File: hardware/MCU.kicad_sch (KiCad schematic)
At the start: 17 parts

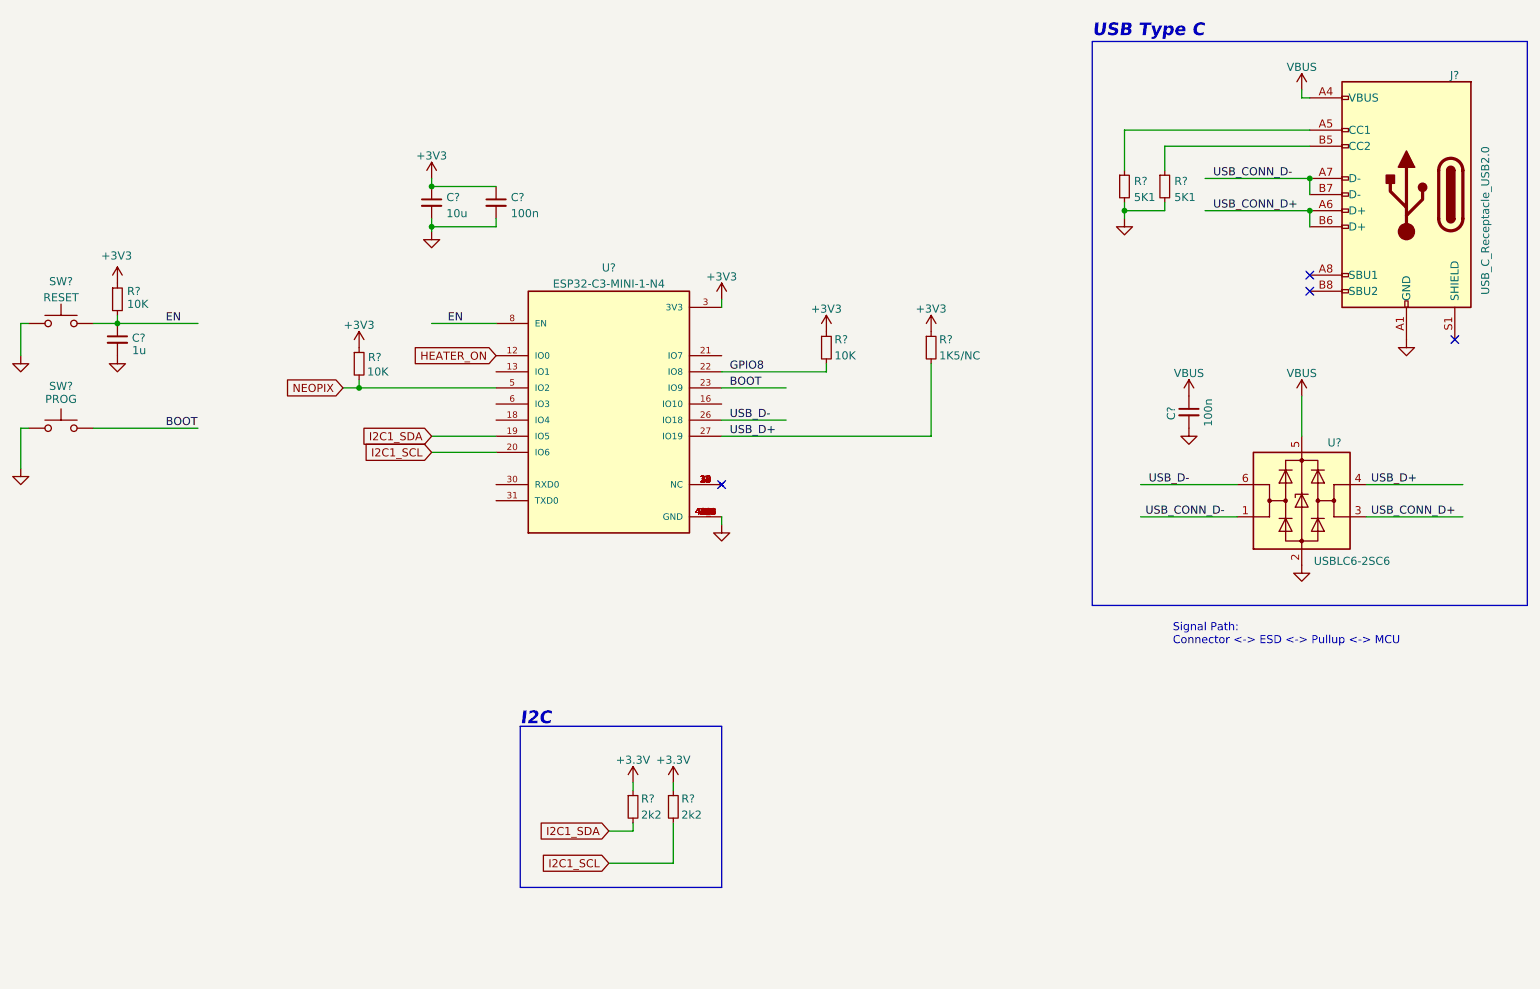
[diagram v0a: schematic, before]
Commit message: schematics finished, footprints assigned. Still need to fix foorptints for MOSFETS
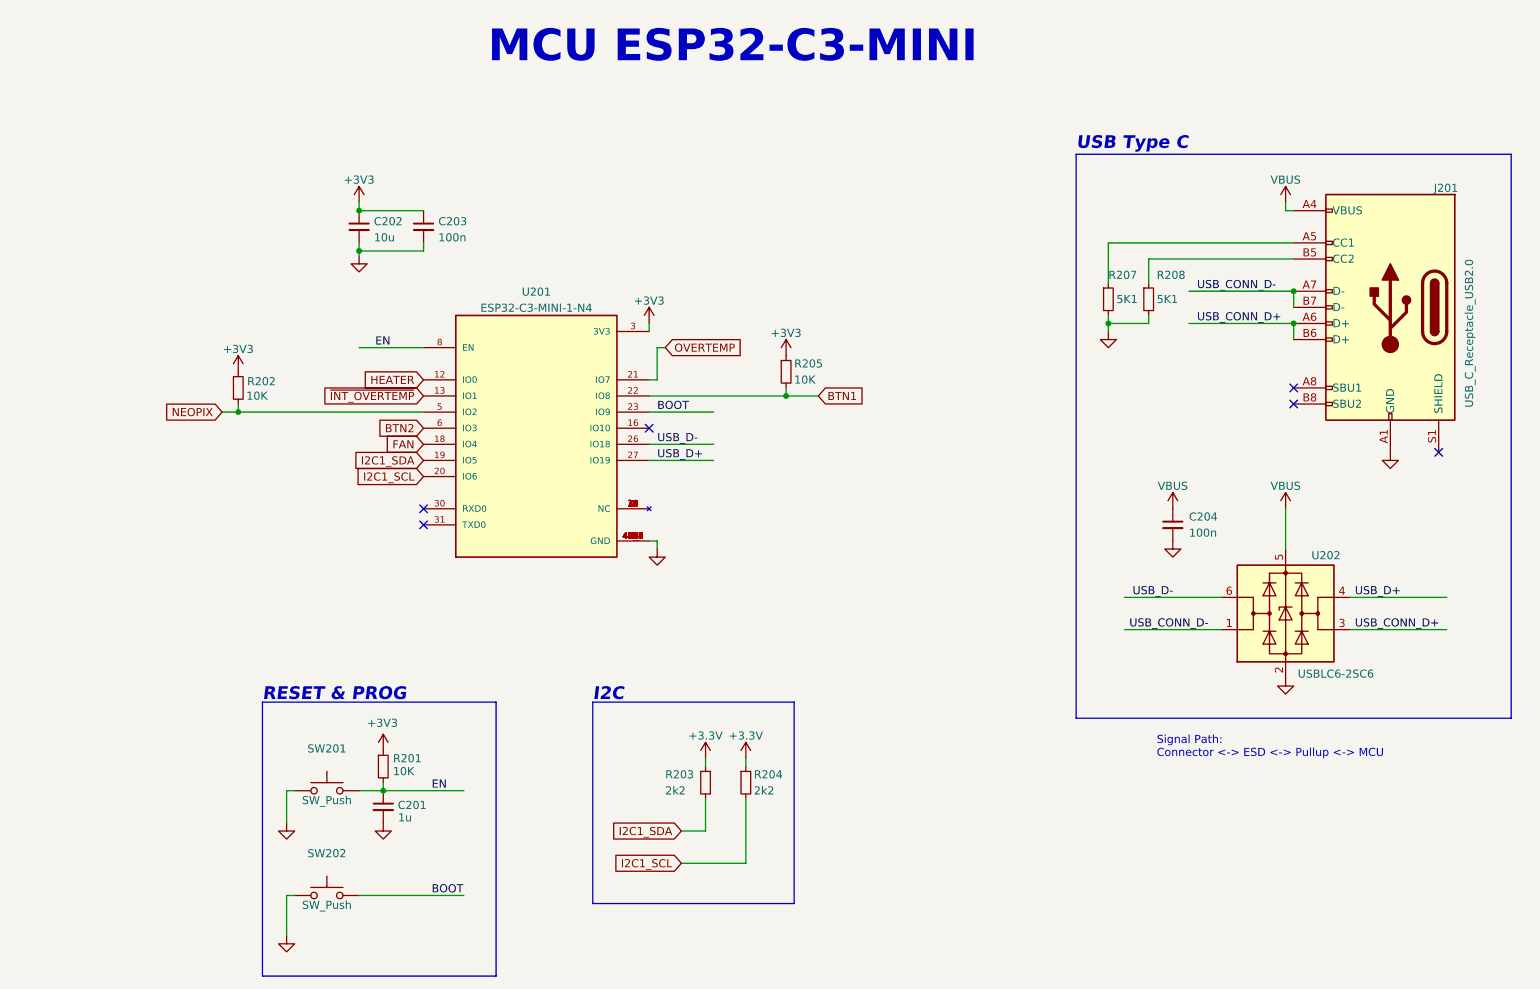
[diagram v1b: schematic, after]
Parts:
- removed R?: 1K5/NC, Resistor_SMD:R_0402_1005Metric, symbol Device:R_Small
- J201: renamed from J?; footprint (none) -> STR-USB:USB_C_Receptacle_C136423
- SW201: renamed from SW?; value RESET -> SW_Push; footprint (none) -> STR-Switch:SW_SMD_SPST_8x3.6; symbol Switch:SW_Push -> STR-Switches:SW_Push
- SW202: renamed from SW?; value PROG -> SW_Push; footprint (none) -> STR-Switch:SW_SMD_SPST_8x3.6; symbol Switch:SW_Push -> STR-Switches:SW_Push
- U201: renamed from U?; footprint esp:ESP32-C3-MINI-1-N4 -> STR-ESP32:ESP32-C3-MINI-1-N4; LCSC (none) -> C2838502; MFPN (none) -> ESP32-C3-MINI-1-N4
- U202: renamed from U?; LCSC (none) -> C2827654; MANUFACTURER (none) -> TECH PUBLIC; MFN (none) -> TECH PUBLIC; MFPN (none) -> USBLC6-2SC6
- gave numbers to parts that had none: 11
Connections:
- net ~{INT_OVERTEMP}: now reaches U201.13 (IO1)
- net FAN: now reaches U201.18 (IO4)
- net OVERTEMP: now reaches U201.21 (IO7)
- net BTN2: now reaches U201.6 (IO3)
- net GPIO8 renamed BTN1
- net HEATER_ON renamed HEATER
- no-connect marks 4 -> 6
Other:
- note added: "MCU ESP32-C3-MINI"
- note added: "RESET & PROG"
- title: (none) -> SLA Chamber Hearter for Resin Printers
- moved on the sheet: C201, C202, C203, C204, J201, R201, R202, R203, R204, R205, R207, R208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

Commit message: routing and foot print changes
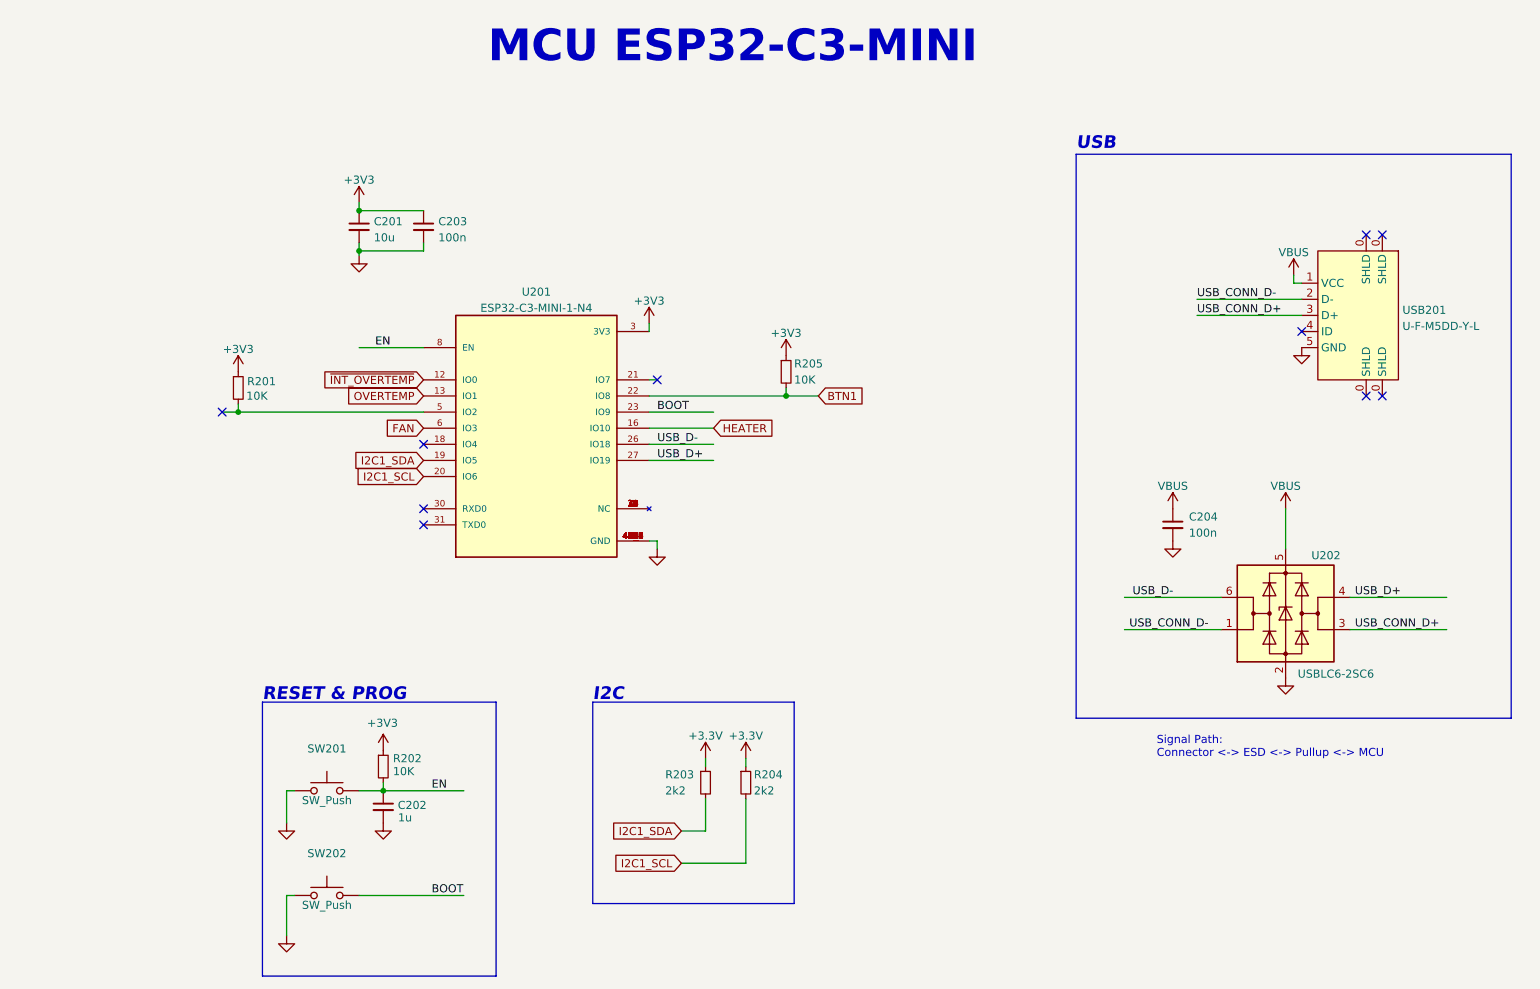
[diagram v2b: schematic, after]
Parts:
- removed J201: USB_C_Receptacle_USB2.0, STR-USB:USB_C_Receptacle_C136423, symbol Connector:USB_C_Receptacle_USB2.0
- removed R207, R208: 5K1, Resistor_SMD:R_0402_1005Metric, symbol Device:R_Small
- added USB201: U-F-M5DD-Y-L, STR-USB:MICRO-USB-SMD_MICRO-USB-18, symbol STR-USB:U-F-M5DD-Y-L
- renumbered C202 to C201, C201 to C202, R202 to R201, R201 to R202
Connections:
- net BTN2 is gone; now on net FAN: U201.6 (IO3)
- net FAN: no longer U201.18 (IO4)
- net GND: now also USB201.5 (GND)
- net HEATER: now also U201.16 (IO10); no longer U201.12 (IO0)
- net OVERTEMP: now also U201.13 (IO1); no longer U201.21 (IO7)
- net USB_CONN_D+: now also USB201.3 (D+)
- net USB_CONN_D-: now also USB201.2 (D-)
- net VBUS: now also USB201.1 (VCC)
- net ~{INT_OVERTEMP}: now also U201.12 (IO0); no longer U201.13 (IO1)
- net NEOPIX: no longer names the net of R201.2, U201.5 (IO2)
- no-connect marks 6 -> 10
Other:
- note added: "USB"
- note removed: "USB Type C"
